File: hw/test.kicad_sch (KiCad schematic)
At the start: 15 parts

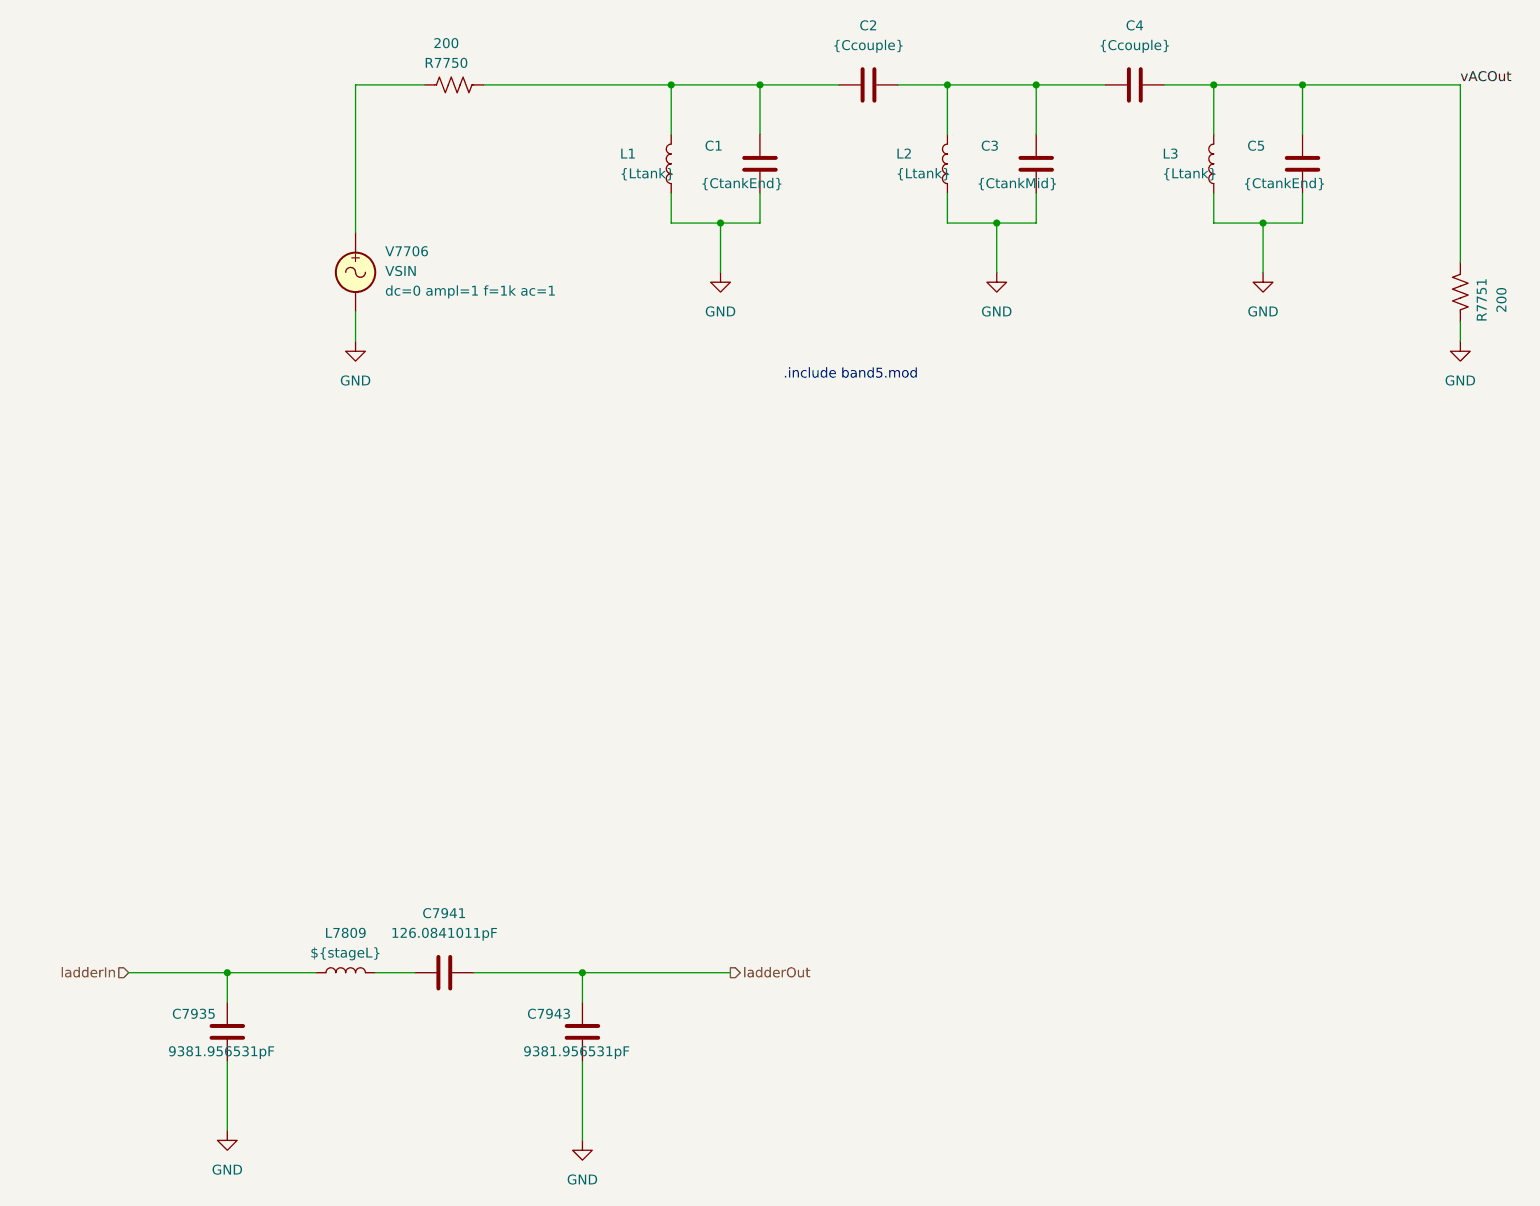
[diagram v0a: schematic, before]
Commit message: Getting closer to having all (ten) BPFs designed. Maybe I can try some layout next.
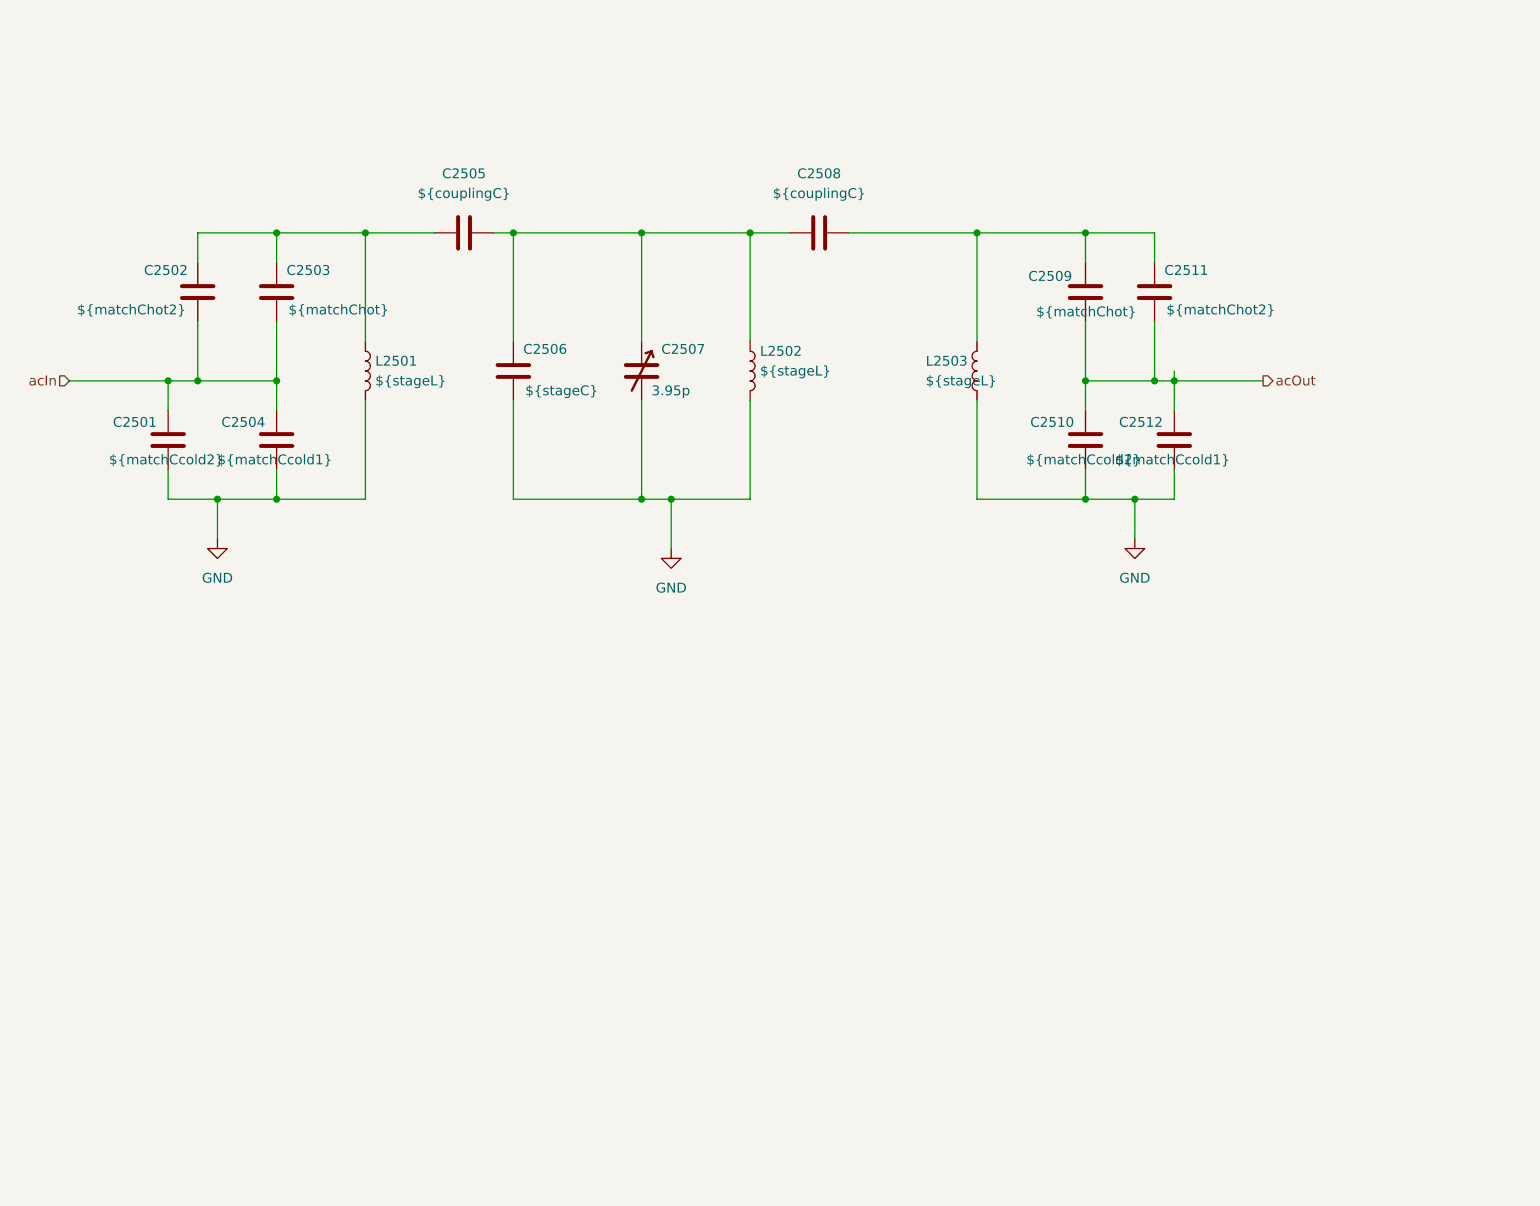
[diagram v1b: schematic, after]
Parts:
- removed C1, C5: {CtankEnd}, symbol Device:C
- removed C4: {Ccouple}, symbol Device:C
- removed C7935, C7943: 9381.956531pF, symbol Device:C
- removed C7941: 126.0841011pF, symbol Device:C
- removed L1, L3: {Ltank}, symbol Device:L
- removed L7809: ${stageL}, symbol Device:L
- removed R7750, R7751: 200, symbol Device:R_US
- removed V7706: VSIN, symbol Simulation_SPICE:VSIN
- added C2501: ${matchCcold2}, symbol Device:C
- added C2502, C2511: ${matchChot2}, symbol Device:C
- added C2503, C2509: ${matchChot}, symbol Device:C
- added C2504, C2512: ${matchCcold1}, symbol Device:C
- added C2505: ${couplingC}, symbol Device:C
- added C2506: ${stageC}, symbol Device:C
- added C2507: 3.95p, PCM_Capacitor_THT_AKL:C_Trimmer_BFC2-808_L7.3mm_W5.5mm_P5.6mm_Hole, symbol PCM_Capacitor_AKL:C_Trim_Vishay_BFC2-808_D7.5mm_Hole
- added L2501, L2502: ${stageL}, symbol Device:L
- C2508: renamed from C2; value {Ccouple} -> ${couplingC}
- C2510: renamed from C3; value {CtankMid} -> ${matchCcold2}
- L2503: renamed from L2; value {Ltank} -> ${stageL}
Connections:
- net GND: now also C2501.2, C2504.2, C2506.2, C2507.2, C2512.2, L2501.2, L2502.2
- net at C2508.1: now also C2505.2, C2506.1, C2507.1, L2502.1
- net at C2508.2, L2503.1: now also C2509.1, C2511.1; no longer C2510.1
- new net: C2502.1, C2503.1, C2505.1, L2501.1
- new net acIn: C2501.1, C2502.2, C2503.2, C2504.1
- new net acOut: C2509.2, C2510.1, C2511.2, C2512.1
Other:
- note removed: ".include band5.mod"
- moved on the sheet: C2508, C2510, L2503
